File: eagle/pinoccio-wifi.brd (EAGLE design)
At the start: 25.4 x 55.4 mm, 17 parts, among them J1 AVR_SPI_PRG_6, U2 LDO-TPS73533

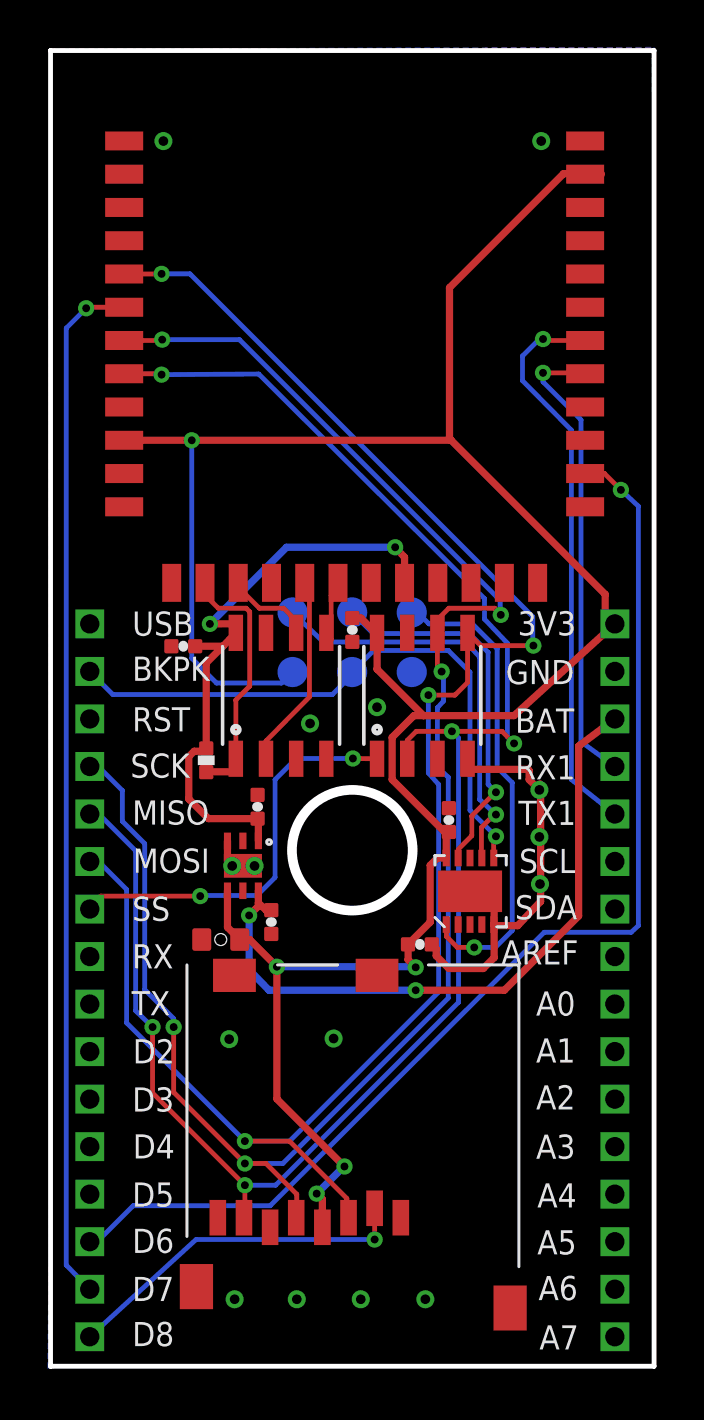
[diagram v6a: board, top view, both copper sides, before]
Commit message: update wifi to v0.13
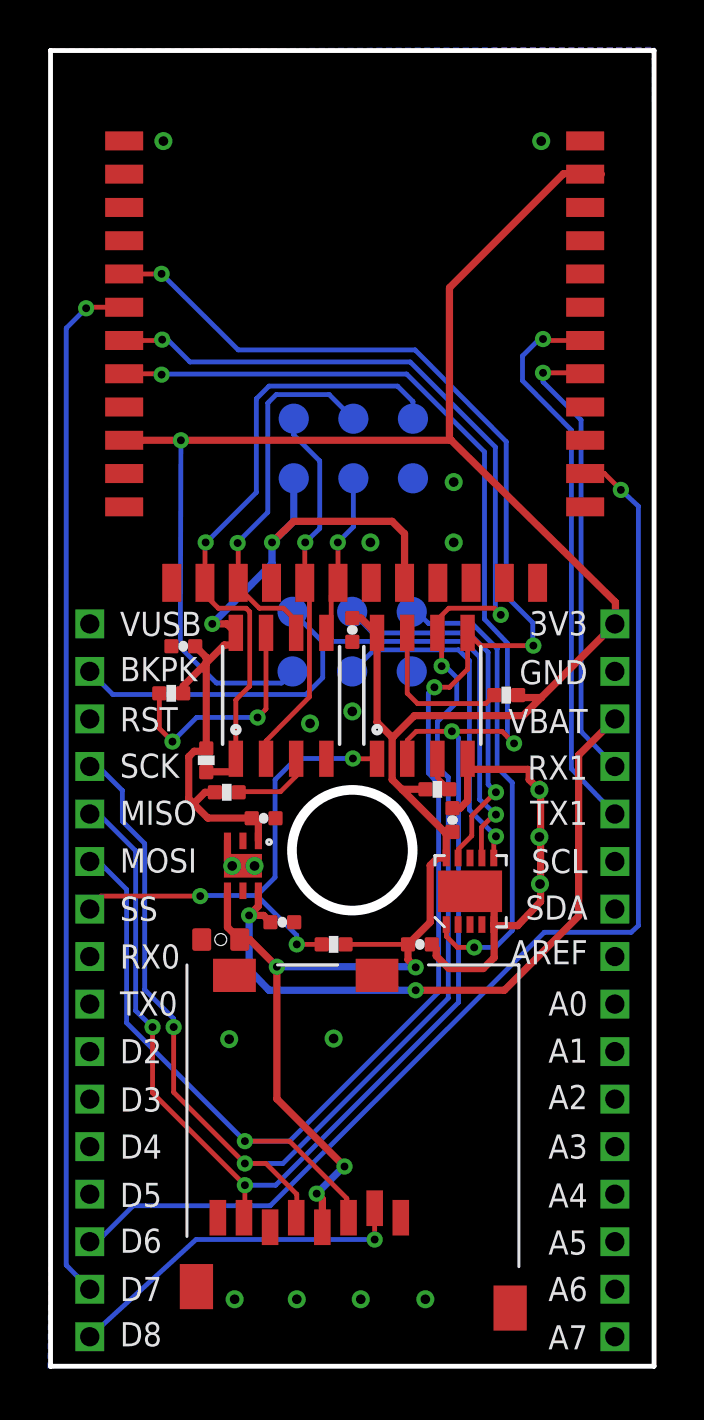
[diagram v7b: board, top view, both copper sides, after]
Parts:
- added J2: AVR_SPI_PRG_6, Pinoccio:2X3-PAD
- added R1, R3, R4, R5, R6: 100k, Pinoccio:0402-RES
- R2: value 10k -> 100k
- moved C2 0.55 mm to (8.97, 31.2), turned to 0 degrees
- moved C1 0.46 mm to (9.75, 26.8), turned to 0 degrees
- moved C7 0.15 mm to (16.9, 31.1)
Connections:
- new net N$1: R3.2, U$4.3
- new net N$5: R4.2, U$4.7
- new net N$6: R6.2, U$2.7
- new net N$7: R5.2, U$2.3
- net BKPK-BUS: now also J1.1, U$3.7; no longer J1.4, U$3.6
- net GND: now also J2.6
- net MSPI-CS: now also J2.5
- net MSPI-MISO: now also J2.1
- net MSPI-MOSI: now also J2.4
- net MSPI-SCK: now also J2.3
- net N$2: now also J1.4, U$3.6; no longer J1.1, U$3.7
- net SSN: now also R1.2
- net VCC-AE: now also R1.1, R5.1, R6.1
- net WIFI-VCC: now also J2.2, R3.1, R4.1
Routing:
- net MSPI-CS: track 11.2 -> 27.7 mm, vias 0 -> 1
- net MSPI-SCK: track 3.72 -> 16.0 mm, vias 0 -> 1
- net N$5: track 0.00 -> 9.97 mm, vias 0 -> 2
- net MSPI-MISO: track 8.23 -> 15.9 mm, vias 0 -> 1
- net WIFI-VCC: track 26.5 -> 33.7 mm
- net N$6: track 0.00 -> 6.54 mm
- net VCC-AE: track 105.7 -> 111.2 mm
- net MSPI-MOSI: track 2.84 -> 7.51 mm, vias 0 -> 1
- net BKPK-BUS: track 25.9 -> 30.2 mm
- net SCK: track 75.3 -> 79.4 mm
- net N$2: track 18.1 -> 14.3 mm
- net SSN: track 17.1 -> 21.0 mm, vias 2 -> 3
- net MISO: track 75.2 -> 78.9 mm
- net N$1: track 0.00 -> 3.43 mm
- net MOSI: track 75.6 -> 79.0 mm
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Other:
- board text added: "2013-08-15"
- board text added: "GS1011 SF"
- board text added: "Pinoccio(tm) Wi-Fi Backpack v1.0"
- board text added: "RX0"
- board text added: "TX0"
- board text added: "VBAT"
- board text added: "VUSB"
- board text added: "wi-fi backpack v1.0"
- board text removed: "BAT"
- board text removed: "Pinoccio(tm) Wi-Fi Backpack v0.13"
- board text removed: "RX"
- board text removed: "TX"
- board text removed: "USB"
- board text removed: "wi-fi backpack v0.13"

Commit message: updated names of components for assembly
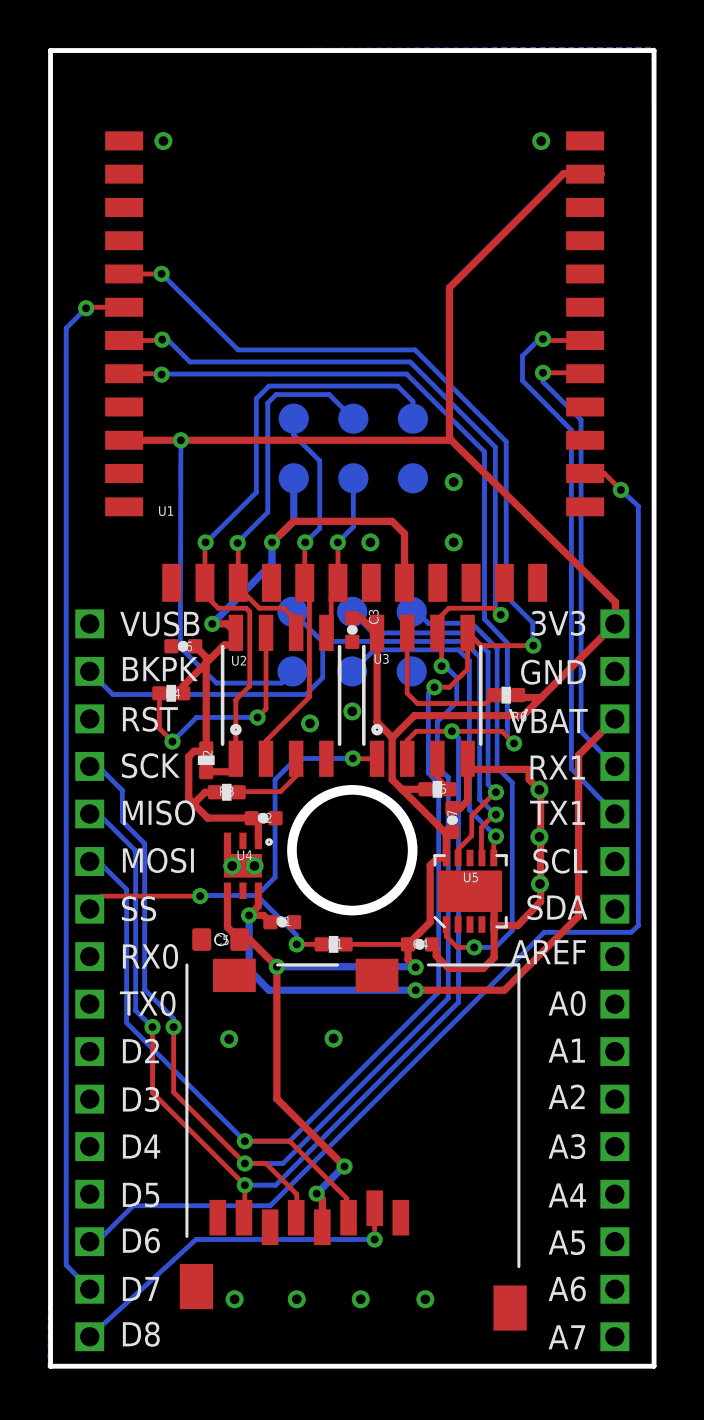
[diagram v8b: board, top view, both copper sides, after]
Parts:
- removed U$4: M25PX16SO8N, Pinoccio:SO8N
- added U4: TPS73533, Pinoccio:SON-6-DRV
- U2: value LDO-TPS73533 -> M25PX16; device Pinoccio:SON-6-DRV -> Pinoccio:SO8N
- U3: value M25PX16SO8N -> M25PX16
- U5: value ATTINY13QFN10 -> ATTINY13A
- moved U2 6.16 mm to (9.70, 36.4), turned to 0 degrees
- renumbered GS1011MIPS to U1, U$2 to U3, U$3 to U5
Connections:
- net GND: now also U2.4, U4.3, U4.PAD; no longer U$4.4, U2.3, U2.PAD
- net MSPI-CS: now also U2.1; no longer U$4.1
- net MSPI-MISO: now also U2.2; no longer U$4.2
- net MSPI-MOSI: now also U2.5; no longer U$4.5
- net MSPI-SCK: now also U2.6; no longer U$4.6
- net N$1: now also U2.3; no longer U$4.3
- net N$5: now also U2.7; no longer U$4.7
- net VBAT: now also U4.6; no longer U2.6
- net VCC-AE: now also U4.4; no longer U2.4
- net WIFI-VCC: now also U2.8, U4.1; no longer U$4.8, U2.1
